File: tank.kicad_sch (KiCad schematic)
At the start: 1 part, among them U1 4001

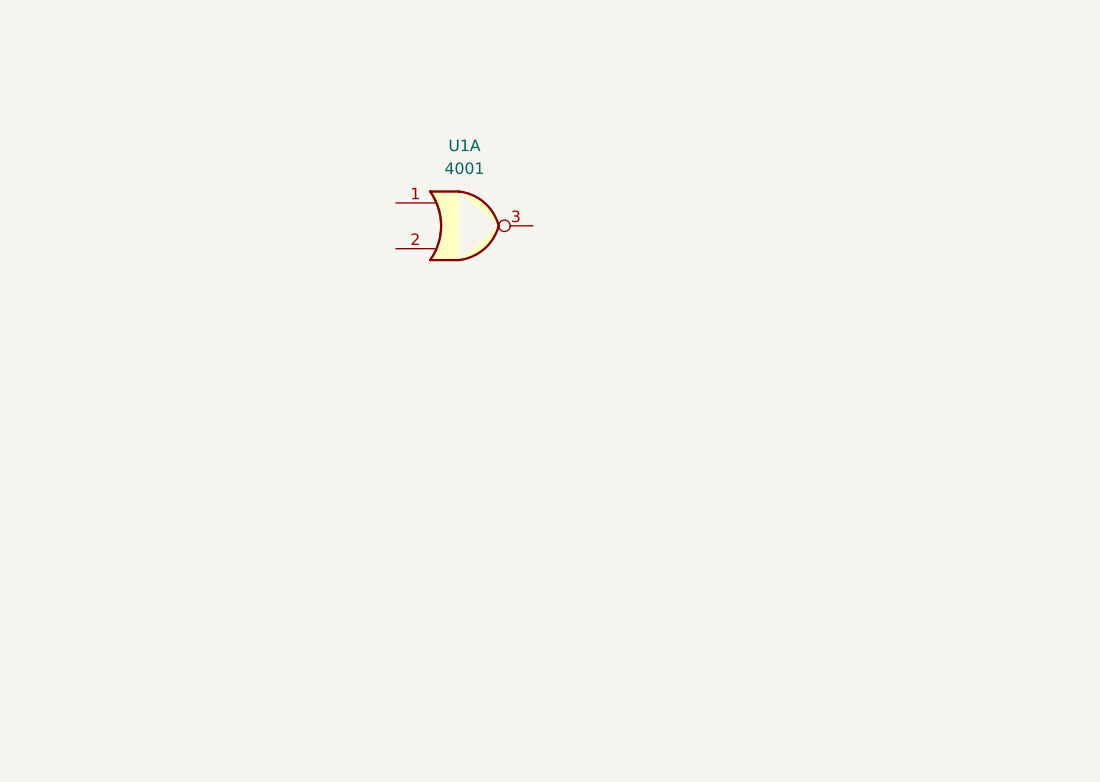
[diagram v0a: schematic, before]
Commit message: Ajouts de 3 feuilles de travail (motors/stm32/power). Ajout de la négociation USB-PD. Ajout d'un régulateur BUCK 3,3V.
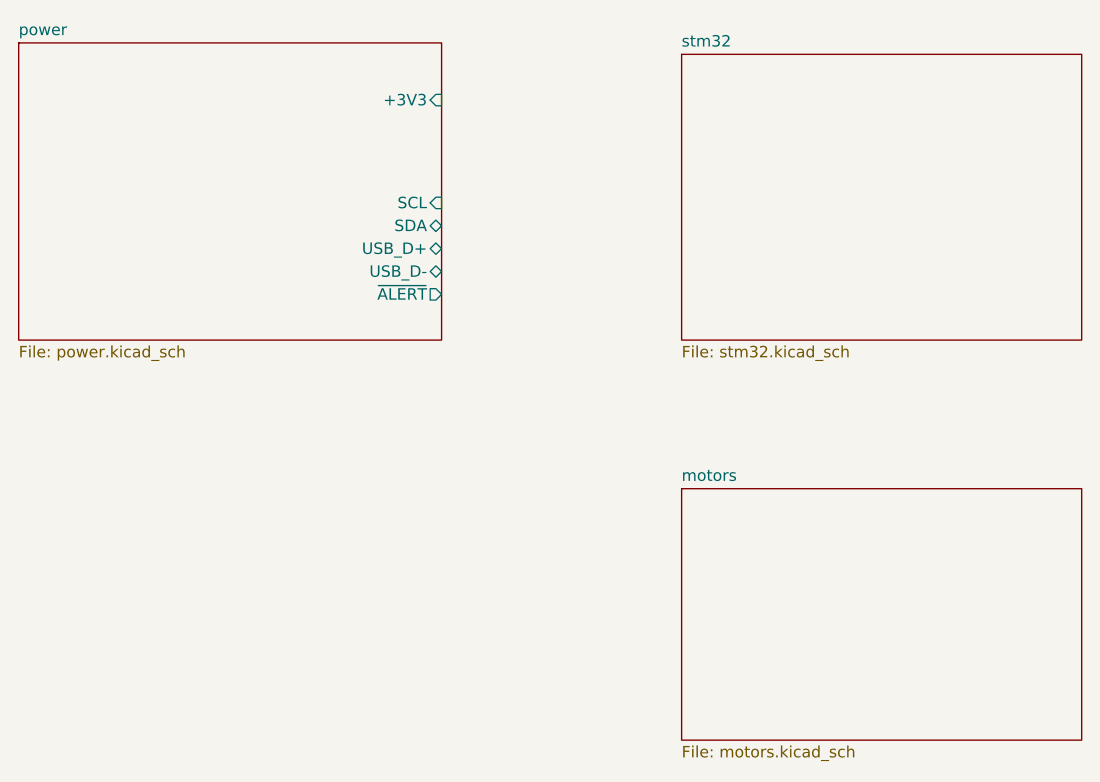
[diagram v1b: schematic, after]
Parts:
- removed U1: 4001, symbol 4xxx:4001
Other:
- added sheet motors (motors.kicad_sch)
- added sheet power (power.kicad_sch)
- added sheet stm32 (stm32.kicad_sch)
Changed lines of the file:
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@@
 	(generator_version "9.0")
 	(paper "A4")
-	(symbol
-		(lib_id "4xxx:4001")
-		(at 107.95 96.52 0)
-		(unit 1)
+	(sheet
+		(at 132.08 77.47)
+		(size 44.45 31.75)
 		(exclude_from_sim no)
 		(in_bom yes)
@@
 		(dnp no)
 		(fields_autoplaced yes)
-		(property "Reference" "U1"
-			(at 107.95 87.63 0)
+		(stroke
+			(width 0.1524)
+			(type solid)
+		)
+		(fill
+			(color 0 0 0 0.0000)
+		)
+		(property "Sheetname" "stm32"
+			(at 132.08 76.7584 0)
 			(effects
 				(font
 					(size 1.27 1.27)
 				)
+				(justify left bottom)
 			)
 		)
-		(property "Value" "4001"
-			(at 107.95 90.17 0)
+		(property "Sheetfile" "stm32.kicad_sch"
+			(at 132.08 109.8046 0)
 			(effects
 				(font
 					(size 1.27 1.27)
 				)
+				(justify left top)
 			)
 		)
-		(property "Footprint" ""
-			(at 107.95 96.52 0)
+		(instances
+			(project "tank"
+				(path "/7245ab6d-141f-4ee3-9edf-0ce22b32345b"
+					(page "3")
+				)
+			)
+		)
+	)
+	(sheet
+		(at 58.42 76.2)
+		(size 46.99 33.02)
+		(exclude_from_sim no)
+		(in_bom yes)
+		(on_board yes)
+		(dnp no)
+		(fields_autoplaced yes)
+		(stroke
+			(width 0.1524)
+			(type solid)
+		)
+		(fill
+			(color 0 0 0 0.0000)
+		)
+		(property "Sheetname" "power"
+			(at 58.42 75.4884 0)
 			(effects
 				(font
 					(size 1.27 1.27)
 				)
-				(hide yes)
+				(justify left bottom)
 			)
 		)
-		(property "Datasheet" "http://www.intersil.com/content/dam/Intersil/documents/cd40/cd4000bms-01bms-02bms-25bms.pdf"
-			(at 107.95 96.52 0)
+		(property "Sheetfile" "power.kicad_sch"
+			(at 58.42 109.8046 0)
 			(effects
 				(font
 					(size 1.27 1.27)
 				)
-				(hide yes)
+				(justify left top)
 			)
 		)
-		(property "Description" "Quad Nor 2 inputs"
-			(at 107.95 96.52 0)
+		(pin "+3V3" input
+			(at 105.41 82.55 0)
 			(effects
 				(font
 					(size 1.27 1.27)
 				)
-				(hide yes)
+				(justify right)
 			)
 		)
-		(pin "3"
+		(pin "SCL" input
+			(at 105.41 93.98 0)
+			(effects
+				(font
+					(size 1.27 1.27)
+				)
+				(justify right)
+			)
 		)
-		(pin "8"
+		(pin "SDA" bidirectional
+			(at 105.41 96.52 0)
+			(effects
+				(font
+					(size 1.27 1.27)
+				)
+				(justify right)
+			)
 		)
-		(pin "6"
+		(pin "USB_D+" bidirectional
+			(at 105.41 99.06 0)
+			(effects
+				(font
+					(size 1.27 1.27)
+				)
+				(justify right)
+			)
 		)
-		(pin "11"
+		(pin "USB_D-" bidirectional
+			(at 105.41 101.6 0)
+			(effects
+				(font
+					(size 1.27 1.27)
+				)
+				(justify right)
+			)
 		)
-		(pin "4"
-		)
-		(pin "1"
-		)
-		(pin "2"
-		)
-		(pin "5"
-		)
-		(pin "9"
-		)
-		(pin "10"
-		)
-		(pin "12"
-		)
-		(pin "13"
-		)
-		(pin "7"
-		)
-		(pin "14"
+		(pin "~{ALERT}" output
+			(at 105.41 104.14 0)
+			(effects
+				(font
+					(size 1.27 1.27)
+				)
+				(justify right)
+			)
 		)
 		(instances
-			(project ""
+			(project "tank"
 				(path "/7245ab6d-141f-4ee3-9edf-0ce22b32345b"
-					(reference "U1")
-					(unit 1)
+					(page "2")
 				)
 			)
+		)
+	)
+	(sheet
+		(at 132.08 125.73)
+		(size 44.45 27.94)
+		(exclude_from_sim no)
+		(in_bom yes)
+		(on_board yes)
+		(dnp no)
+		(fields_autoplaced yes)
+		(stroke
+			(width 0.1524)
+			(type solid)
+		)
+		(fill
+			(color 0 0 0 0.0000)
+		)
+		(property "Sheetname" "motors"
+			(at 132.08 125.0184 0)
+			(effects
+				(font
+					(size 1.27 1.27)
+				)
+				(justify left bottom)
+			)
+		)
+		(property "Sheetfile" "motors.kicad_sch"
+			(at 132.08 154.2546 0)
+			(effects
+				(font
+					(size 1.27 1.27)
+				)
+				(justify left top)
+			)
+		)
+		(instances
+			(project "tank"
+				(path "/7245ab6d-141f-4ee3-9edf-0ce22b32345b"
+					(page "4")
+				)
+			)

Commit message: Ajout des deux moteurs
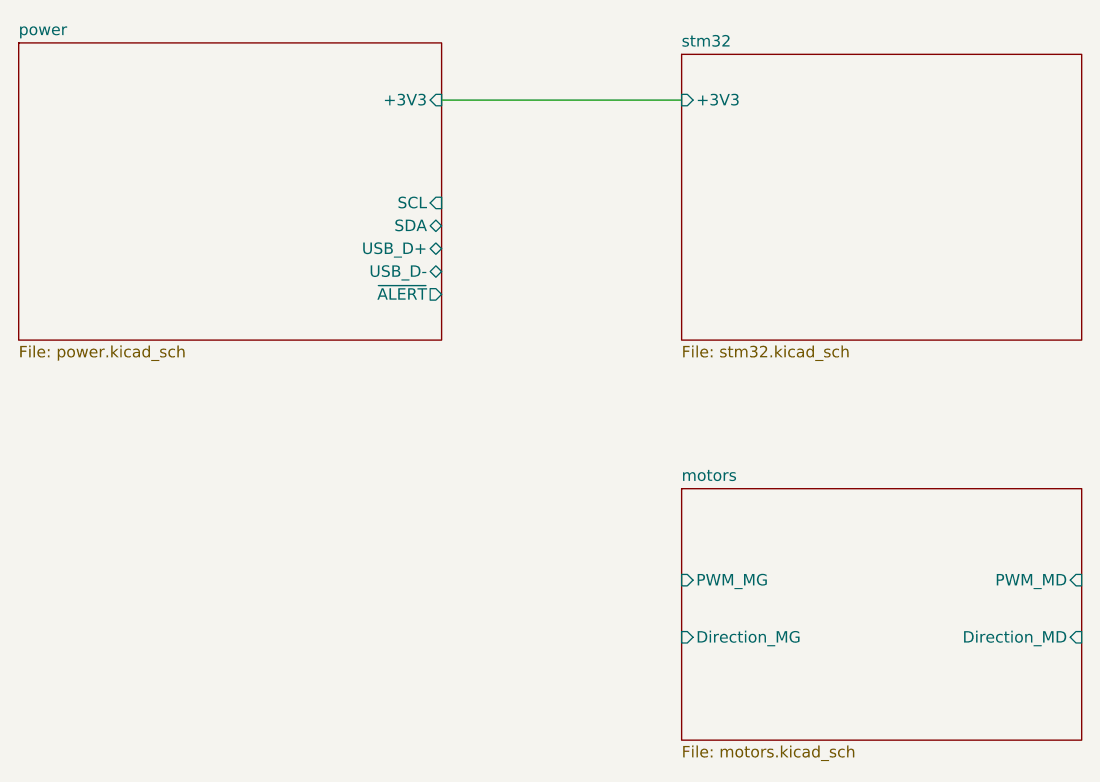
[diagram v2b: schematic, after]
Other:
- sheet motors ports: added Direction_MD, Direction_MG, PWM_MD, PWM_MG; removed none
- sheet stm32 ports: added +3V3; removed none
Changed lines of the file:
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@@
 	(generator_version "9.0")
 	(paper "A4")
+	(wire
+		(pts
+			(xy 105.41 82.55) (xy 132.08 82.55)
+		)
+		(stroke
+			(width 0)
+			(type default)
+		)
+	)
 	(sheet
 		(at 132.08 77.47)
@@
 				)
 				(justify left top)
+			)
+		)
+		(pin "+3V3" input
+			(at 132.08 82.55 180)
+			(effects
+				(font
+					(size 1.27 1.27)
+				)
+				(justify left)
 			)
 		)
@@
 			)
 		)
+		(pin "PWM_MG" input
+			(at 132.08 135.89 180)
+			(effects
+				(font
+					(size 1.27 1.27)
+				)
+				(justify left)
+			)
+		)
+		(pin "Direction_MD" input
+			(at 176.53 142.24 0)
+			(effects
+				(font
+					(size 1.27 1.27)
+				)
+				(justify right)
+			)
+		)
+		(pin "Direction_MG" input
+			(at 132.08 142.24 180)
+			(effects
+				(font
+					(size 1.27 1.27)
+				)
+				(justify left)
+			)
+		)
+		(pin "PWM_MD" input
+			(at 176.53 135.89 0)
+			(effects
+				(font
+					(size 1.27 1.27)
+				)
+				(justify right)
+			)
+		)
